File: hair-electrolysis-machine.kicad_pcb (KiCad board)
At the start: 2 copper layers, 53 x 53 mm, 82 parts, among them J1 Conn_01x04_Pin, J2 USB_C_Receptacle_USB2.0_16P, J3 AudioJack2_Ground_Switch, J4 Conn_01x04_Pin, J5 Conn_01x04_Pin, J6 AudioJack2_Ground_Switch, J7 AudioJack2_Ground_Switch, Q1 BSS138, SW1 SW_SPDT, SW2 BTN, SW3 BTN, SW4 RotaryEncoder_Switch, SW5 BTN, U1 TP4054, U2 XC6206PxxxMR, U3 LM358B, U4 STM32G0B1RBTx

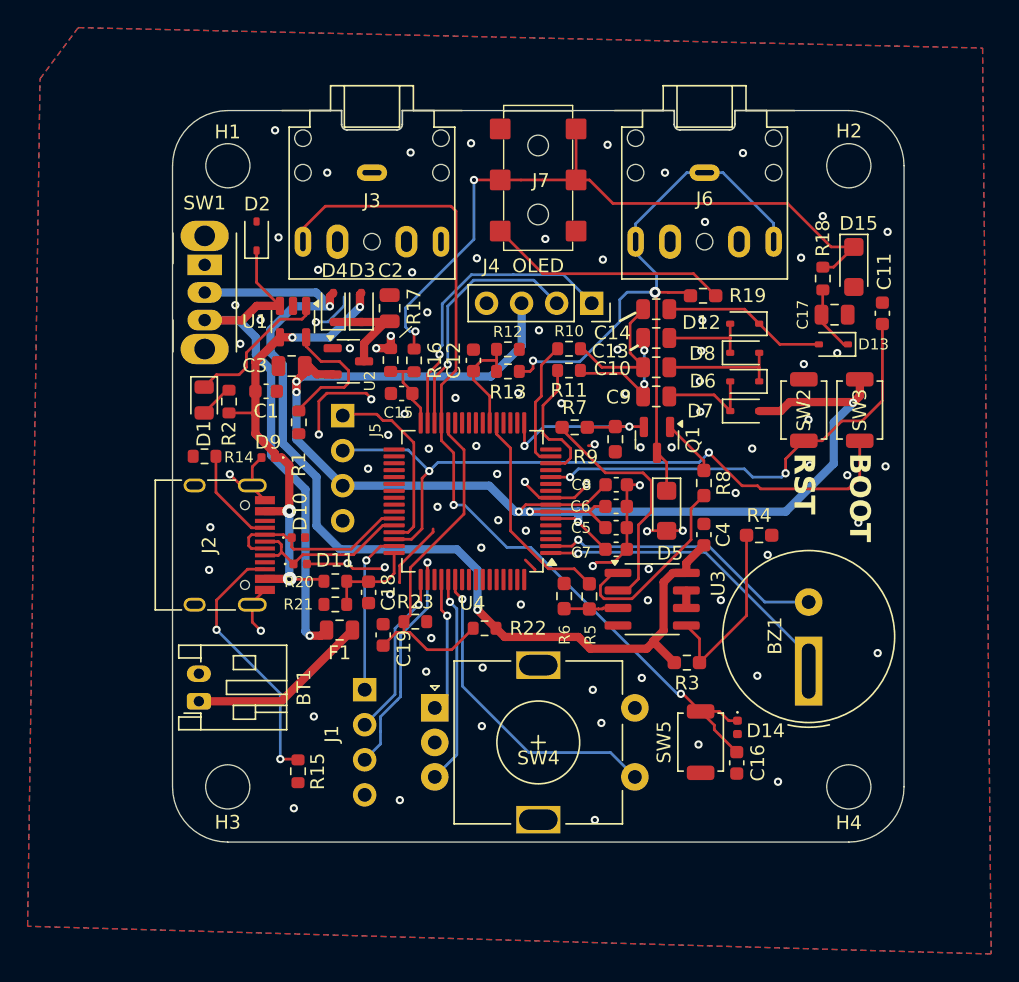
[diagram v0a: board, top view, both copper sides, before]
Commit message: Silkscreen edits and moved F1 to more maintainable spot
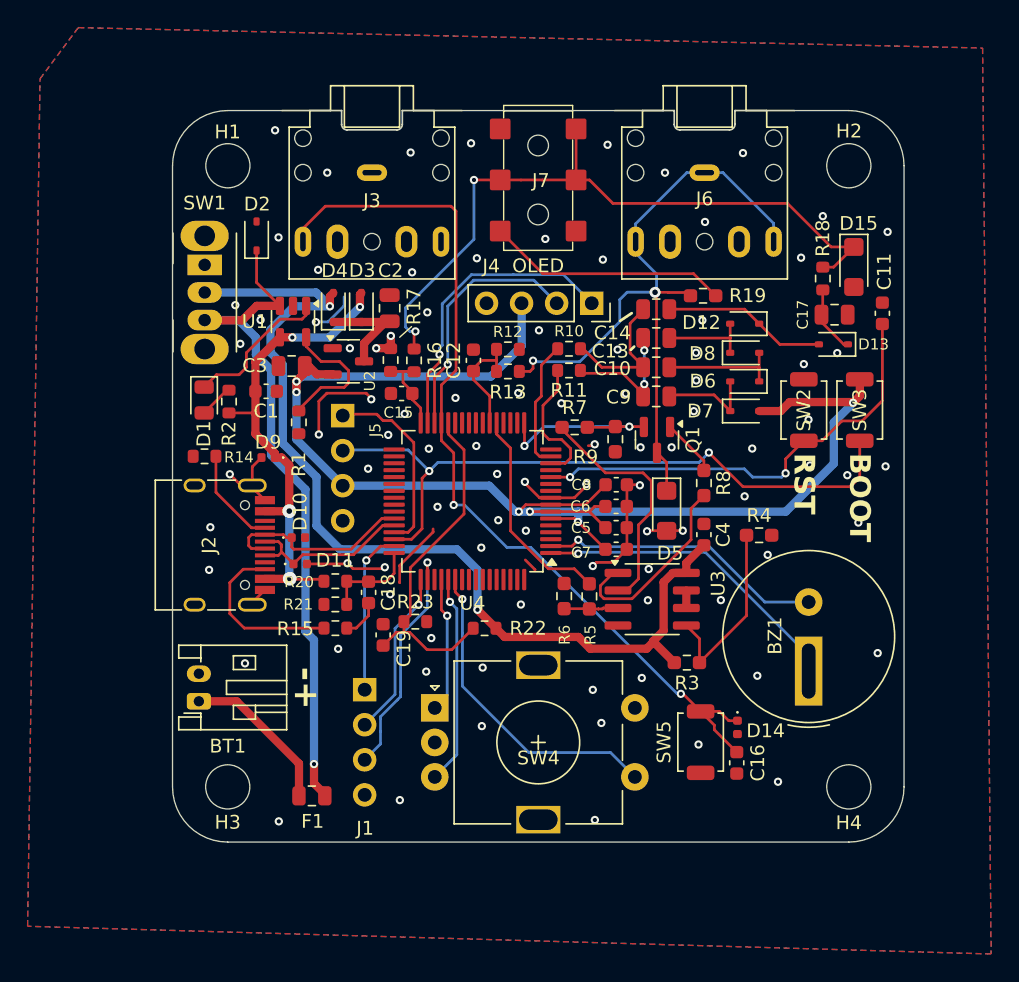
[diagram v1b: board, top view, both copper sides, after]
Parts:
- moved F1 12.2 mm to (133.1, 120.7), turned to 0 degrees
- moved R15 10.7 mm to (134.8, 108.5), turned to 0 degrees
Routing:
- net Net-(D2-K): track 38.9 -> 49.5 mm
- net Net-(J2-CC2): track 19.2 -> 12.5 mm, vias 2 -> 0
- net Net-(BT1-+): track 13.3 -> 11.5 mm
- net GND: track 50.8 -> 51.5 mm
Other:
- board text added: "GND 3v3 SCL SDA"
- board text added: "Mod me here!"
- board text added: "scd31.com"

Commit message: Added wire routing hole
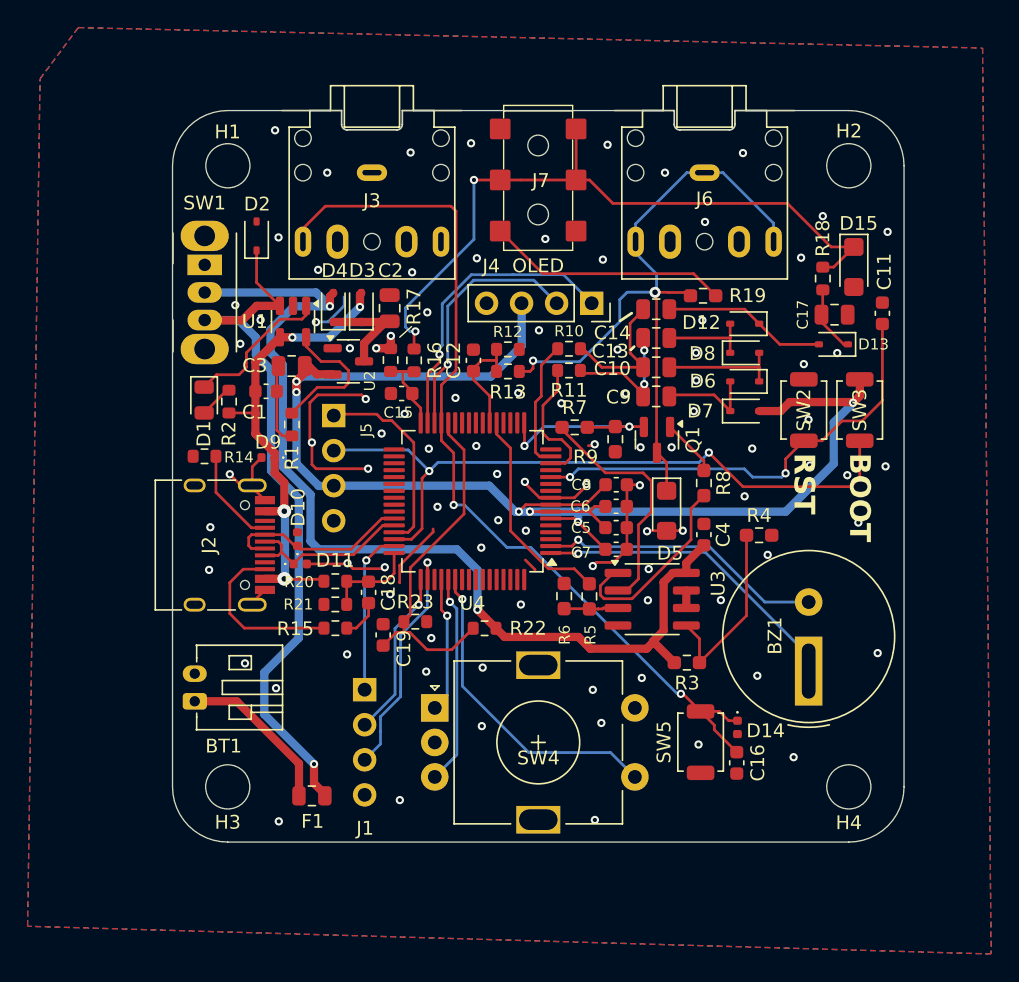
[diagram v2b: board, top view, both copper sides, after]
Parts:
- added H5: MountingHole, MountingHole:MountingHole_2.5mm, F.Cu at (133.4, 112.8)
- moved J5 0.65 mm to (134.7, 93.1)
- moved R1 0.52 mm to (131.7, 93.8)
- moved BT1 0.30 mm to (124.6, 113.8)
- moved D10 0.13 mm to (132.1, 102.0), turned to 90 degrees
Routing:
- net GND: track 51.5 -> 64.0 mm, vias 92 -> 93
- net Net-(D2-K): track 49.5 -> 51.6 mm
- net +3.3V: track 105.7 -> 106.7 mm
- net +BATT: track 71.8 -> 72.7 mm
- net +5V: track 35.6 -> 34.7 mm
- net Net-(BT1-+): track 11.5 -> 12.1 mm
- net Net-(U1-PROG): track 10.2 -> 10.7 mm
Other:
- board text added: "Based on n3tcat's design scd31.com"
- board text removed: "scd31.com"

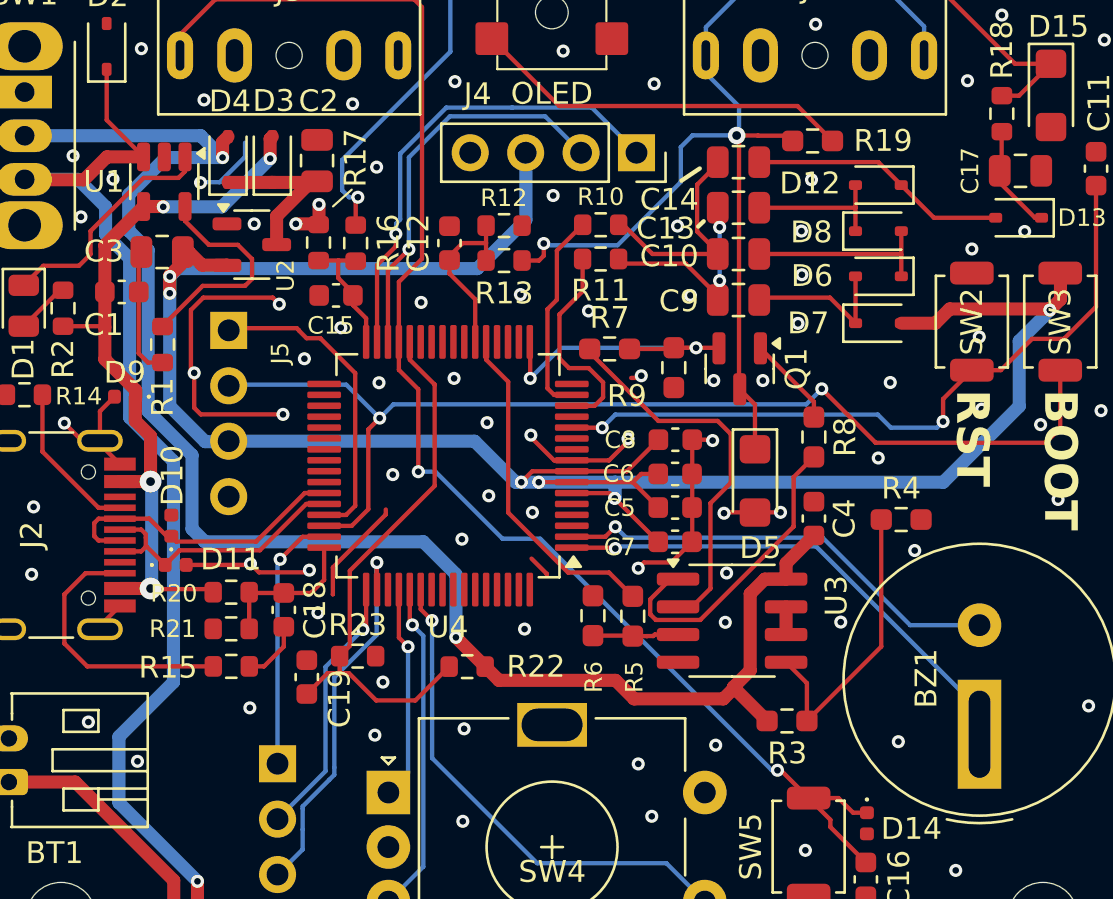
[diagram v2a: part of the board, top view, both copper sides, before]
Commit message: Make buzzer single sided for simplicity
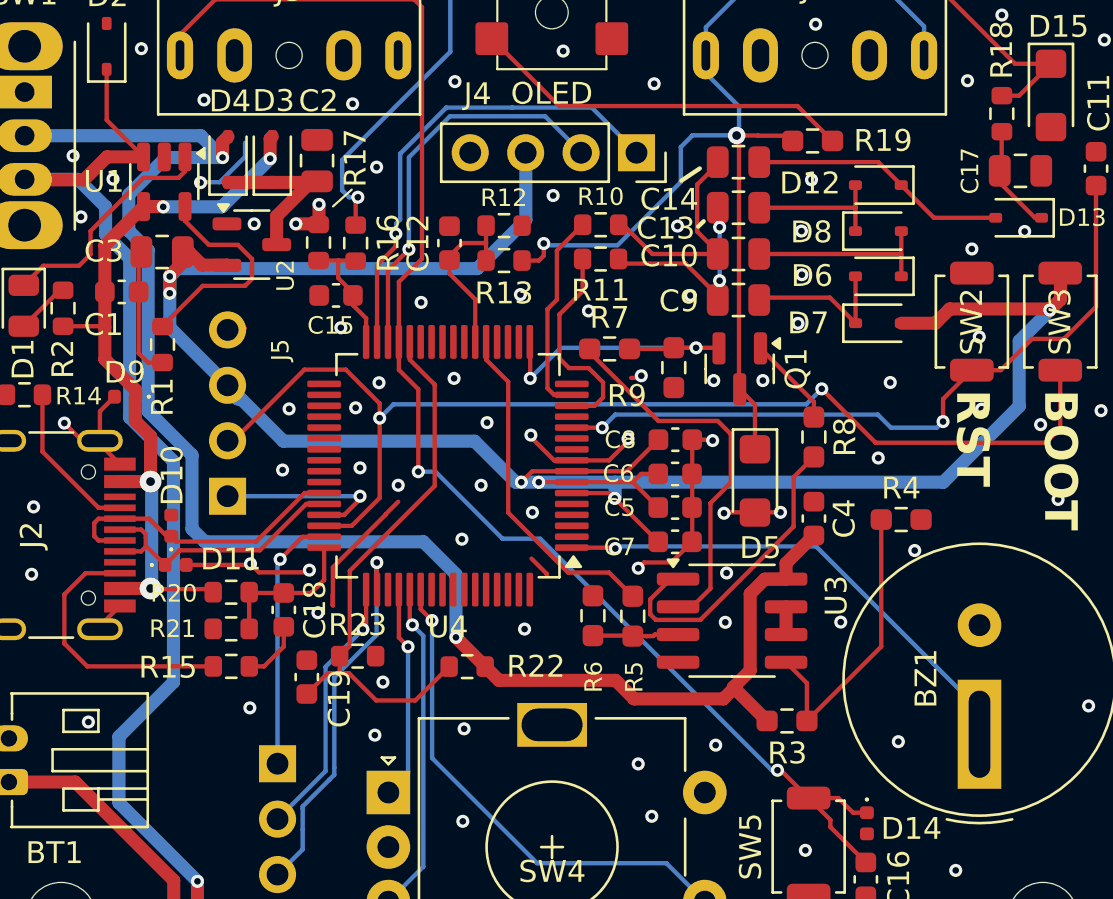
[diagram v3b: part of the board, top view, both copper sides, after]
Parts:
- moved J5 7.60 mm to (134.6, 100.7), turned to 180 degrees
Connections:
- BZ1 pad 2: /Mcu/BUZZER2 -> GND
- U4 pad 2: /Mcu/BUZZER2 -> unconnected-(U4-PC12-Pad2)
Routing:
- net /Mcu/BUZZER2: track 20.7 -> 0.00 mm, vias 1 -> 0
- net GND: track 64.0 -> 52.5 mm, vias 93 -> 92
- net SWDIO: track 13.7 -> 8.15 mm, vias 0 -> 1
- net SWCLK: track 49.4 -> 52.1 mm
- net +3.3V: track 106.7 -> 104.7 mm
